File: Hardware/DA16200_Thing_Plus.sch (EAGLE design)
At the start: 61 parts, among them J2 THING_PLUS, J3 Qwiic, J5 USB C, J6 microSD, J7 CORTEX_JTAG_DEBUG_PTH_NS, Q1 20V/4.2A/52mΩ/1.4W, U1 DA16200MOD, U2 CH340E_MSOP10, U3 MCP73831, U5 4MB Flash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

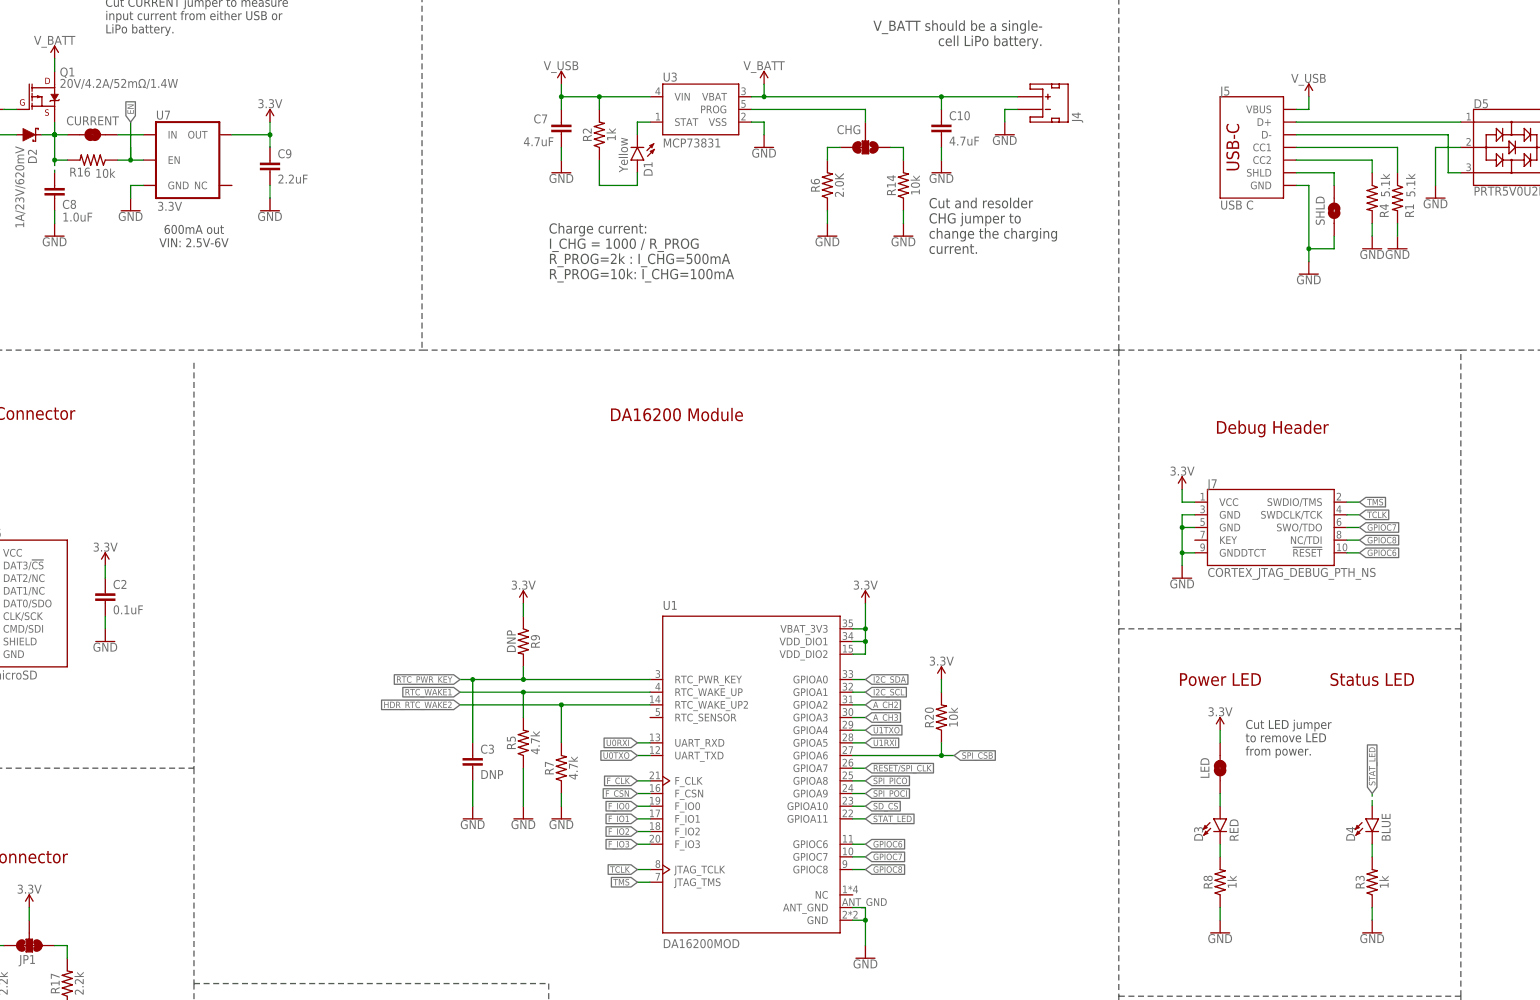
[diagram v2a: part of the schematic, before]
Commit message: Design review updates
Schematic:
* Re-wire wakeup pins to match app schematic and previous designs
* Change SHLD jumper to NC
* Remove "ANT_GND" pin label from DA16200 symbol
Board:
* Draw polygon to connect shield pins of USBC connector on top and bottom
* Rename button GPIOC7
* Breakout JTAG pins to TPs on the bottom
* Redraw polygons for middle layers to avoid the antenna GND keepout
* Fixed LED label on the jumper and the pin
* Changed "CURR" label to "MEAS"
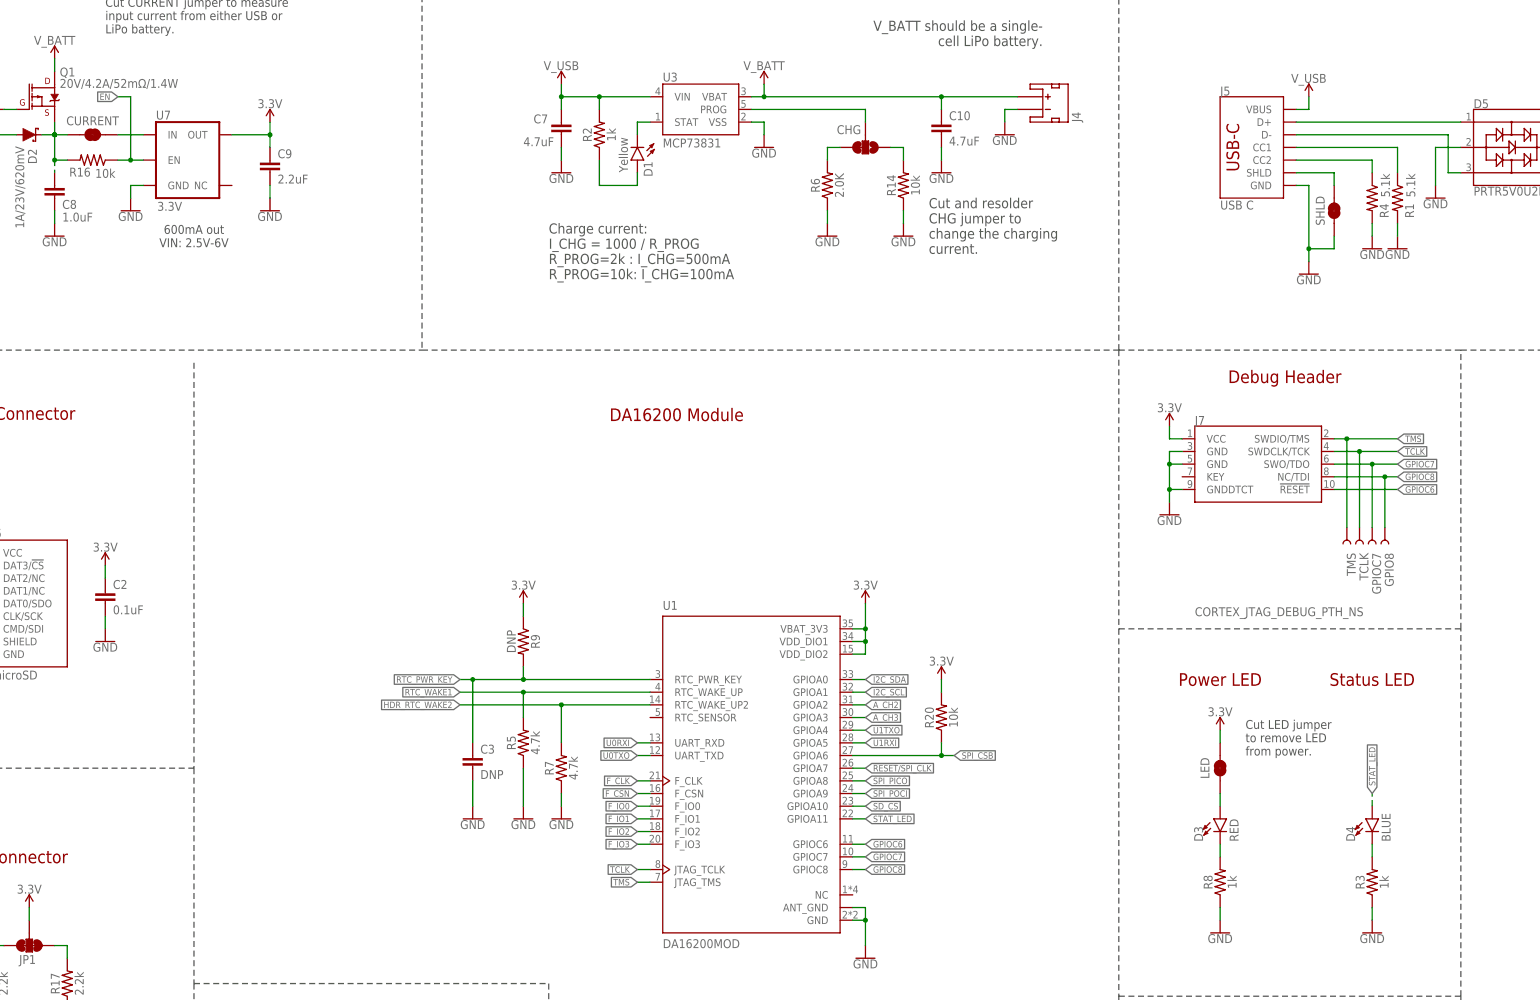
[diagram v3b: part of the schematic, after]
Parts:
- added GPIO8, GPIOC7, TCLK, TMS: TEST-POINT3, SparkFun-Connectors:TEST-POINT3
- SHLD: value JUMPER-SMT_2_NO_SILK -> JUMPER-SMT_2_NC_TRACE_SILK; device SparkFun-Jumpers:JUMPER-SMT_2_NO_SILK -> SparkFun-Jumpers:JUMPER-SMT_2_NC_TRACE_SILK
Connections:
- net GPIOC7: now also GPIOC7.1
- net GPIOC8: now also GPIO8.1
- net TCLK: now also TCLK.1
- net TMS: now also TMS.1
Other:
- moved on the sheet: J7
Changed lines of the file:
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@@
 <?xml version="1.0" encoding="utf-8"?>
 <!DOCTYPE eagle SYSTEM "eagle.dtd">
-<eagle version="9.5.2">
+<eagle version="9.4.2">
 <drawing>
 <settings>
-<setting alwaysvectorfont="no"/>
+<setting alwaysvectorfont="yes"/>
 <setting keepoldvectorfont="yes"/>
 <setting verticaltext="up"/>
@@
 <part name="GND22" library="SparkFun-PowerSymbols" deviceset="GND" device=""/>
 <part name="R18" library="SparkFun-Resistors" deviceset="100OHM" device="-0402-TIGHT-1/16W-1%" value="100"/>
-<part name="SHLD" library="SparkFun-Jumpers" deviceset="JUMPER-SMT_2_NO" device="_SILK" package3d_urn="urn:adsk.eagle:package:39279/1"/>
+<part name="SHLD" library="SparkFun-Jumpers" deviceset="JUMPER-SMT_2_NC_TRACE" device="_SILK" package3d_urn="urn:adsk.eagle:package:39281/1"/>
 <part name="GND23" library="SparkFun-PowerSymbols" deviceset="GND" device=""/>
 <part name="GND24" library="SparkFun-PowerSymbols" deviceset="GND" device=""/>
@@
 <part name="SUPPLY18" library="SparkFun-PowerSymbols" deviceset="3.3V" device=""/>
 <part name="SUPPLY19" library="SparkFun-PowerSymbols" deviceset="3.3V" device=""/>
+<part name="TMS" library="SparkFun-Connectors" deviceset="TEST-POINT" device="3"/>
+<part name="TCLK" library="SparkFun-Connectors" deviceset="TEST-POINT" device="3"/>
+<part name="GPIOC7" library="SparkFun-Connectors" deviceset="TEST-POINT" device="3"/>
+<part name="GPIO8" library="SparkFun-Connectors" deviceset="TEST-POINT" device="3"/>
 </parts>
 <sheets>
@@
 <text x="40.64" y="180.34" size="2.54" layer="94" font="vector" align="center">uSD Connector</text>
 <wire x1="261.62" y1="193.04" x2="261.62" y2="279.4" width="0.2032" layer="97" style="longdash"/>
-<text x="292.354" y="177.546" size="2.54" layer="94" font="vector" align="center">Debug Header</text>
+<text x="294.894" y="187.706" size="2.54" layer="94" font="vector" align="center">Debug Header</text>
 <text x="281.94" y="127" size="2.54" layer="94" font="vector" align="center">Power LED</text>
 <text x="355.6" y="10.16" size="2.54" layer="94" font="vector">Priyanka Makin</text>
@@
 <attribute name="VALUE" x="421.64" y="228.346" size="1.778" layer="96" align="top-center"/>
 </instance>
-<instance part="J7" gate="J1" x="292.1" y="157.48" smashed="yes">
-<attribute name="NAME" x="279.4" y="165.354" size="1.778" layer="95" font="vector"/>
-<attribute name="VALUE" x="279.4" y="147.574" size="1.778" layer="96" font="vector"/>
-</instance>
-<instance part="SUPPLY13" gate="G$1" x="274.32" y="165.1" smashed="yes">
-<attribute name="VALUE" x="274.32" y="167.894" size="1.778" layer="96" align="bottom-center"/>
-</instance>
-<instance part="GND16" gate="1" x="274.32" y="147.32" smashed="yes">
-<attribute name="VALUE" x="274.32" y="147.066" size="1.778" layer="96" align="top-center"/>
+<instance part="J7" gate="J1" x="289.56" y="170.18" smashed="yes">
+<attribute name="NAME" x="276.86" y="178.054" size="1.778" layer="95" font="vector"/>
+<attribute name="VALUE" x="276.86" y="139.7" size="1.778" layer="96" font="vector"/>
+</instance>
+<instance part="SUPPLY13" gate="G$1" x="271.78" y="177.8" smashed="yes">
+<attribute name="VALUE" x="271.78" y="180.594" size="1.778" layer="96" align="bottom-center"/>
+</instance>
+<instance part="GND16" gate="1" x="271.78" y="160.02" smashed="yes">
+<attribute name="VALUE" x="271.78" y="159.766" size="1.778" layer="96" align="top-center"/>
 </instance>
 <instance part="R5" gate="G$1" x="142.24" y="114.3" smashed="yes" rot="R90">
@@
 <instance part="SUPPLY19" gate="G$1" x="226.06" y="127" smashed="yes">
 <attribute name="VALUE" x="226.06" y="129.794" size="1.778" layer="96" align="bottom-center"/>
+</instance>
+<instance part="TMS" gate="G$1" x="307.34" y="157.48" smashed="yes" rot="R270">
+<attribute name="NAME" x="307.34" y="152.4" size="1.778" layer="95" font="vector" rot="R270"/>
+</instance>
+<instance part="TCLK" gate="G$1" x="309.88" y="157.48" smashed="yes" rot="R270">
+<attribute name="NAME" x="309.88" y="152.4" size="1.778" layer="95" font="vector" rot="R270"/>
+</instance>
+<instance part="GPIOC7" gate="G$1" x="312.42" y="157.48" smashed="yes" rot="R270">
+<attribute name="NAME" x="312.42" y="152.4" size="1.778" layer="95" font="vector" rot="R270"/>
+</instance>
+<instance part="GPIO8" gate="G$1" x="314.96" y="157.48" smashed="yes" rot="R270">
+<attribute name="NAME" x="314.96" y="152.4" size="1.778" layer="95" font="vector" rot="R270"/>
 </instance>
 </instances>
@@
 <segment>
 <pinref part="J7" gate="J1" pin="VCC"/>
-<wire x1="276.86" y1="162.56" x2="274.32" y2="162.56" width="0.1524" layer="91"/>
-<wire x1="274.32" y1="162.56" x2="274.32" y2="165.1" width="0.1524" layer="91"/>
+<wire x1="274.32" y1="175.26" x2="271.78" y2="175.26" width="0.1524" layer="91"/>
+<wire x1="271.78" y1="175.26" x2="271.78" y2="177.8" width="0.1524" layer="91"/>
 <pinref part="SUPPLY13" gate="G$1" pin="3.3V"/>
 </segment>
@@
 <segment>
 <pinref part="J7" gate="J1" pin="GND@3"/>
-<wire x1="276.86" y1="160.02" x2="274.32" y2="160.02" width="0.1524" layer="91"/>
-<wire x1="274.32" y1="160.02" x2="274.32" y2="157.48" width="0.1524" layer="91"/>
+<wire x1="274.32" y1="172.72" x2="271.78" y2="172.72" width="0.1524" layer="91"/>
+<wire x1="271.78" y1="172.72" x2="271.78" y2="170.18" width="0.1524" layer="91"/>
 <pinref part="J7" gate="J1" pin="GND@5"/>
-<wire x1="274.32" y1="157.48" x2="274.32" y2="152.4" width="0.1524" layer="91"/>
-<wire x1="274.32" y1="152.4" x2="274.32" y2="149.86" width="0.1524" layer="91"/>
-<wire x1="276.86" y1="157.48" x2="274.32" y2="157.48" width="0.1524" layer="91"/>
-<junction x="274.32" y="157.48"/>
+<wire x1="271.78" y1="170.18" x2="271.78" y2="165.1" width="0.1524" layer="91"/>
+<wire x1="271.78" y1="165.1" x2="271.78" y2="162.56" width="0.1524" layer="91"/>
+<wire x1="274.32" y1="170.18" x2="271.78" y2="170.18" width="0.1524" layer="91"/>
+<junction x="271.78" y="170.18"/>
 <pinref part="J7" gate="J1" pin="GNDDTCT"/>
-<wire x1="274.32" y1="152.4" x2="276.86" y2="152.4" width="0.1524" layer="91"/>
-<junction x="274.32" y="152.4"/>
+<wire x1="271.78" y1="165.1" x2="274.32" y2="165.1" width="0.1524" layer="91"/>
+<junction x="271.78" y="165.1"/>
 <pinref part="GND16" gate="1" pin="GND"/>
 </segment>
@@
 <segment>
 <wire x1="66.04" y1="231.14" x2="63.5" y2="231.14" width="0.1524" layer="91"/>
-<wire x1="63.5" y1="231.14" x2="60.96" y2="231.14" width="0.1524" layer="91"/>
-<wire x1="63.5" y1="238.76" x2="63.5" y2="231.14" width="0.1524" layer="91"/>
-<wire x1="63.5" y1="233.68" x2="63.5" y2="231.14" width="0.1524" layer="91"/>
-<junction x="63.5" y="231.14"/>
-<label x="63.5" y="238.76" size="1.27" layer="95" font="vector" rot="R90" xref="yes"/>
 <pinref part="U7" gate="G$1" pin="EN"/>
 <pinref part="R16" gate="G$1" pin="1"/>
+<wire x1="63.5" y1="231.14" x2="60.96" y2="231.14" width="0.1524" layer="91"/>
+<wire x1="63.5" y1="231.14" x2="63.5" y2="243.84" width="0.1524" layer="91"/>
+<junction x="63.5" y="231.14"/>
+<wire x1="63.5" y1="243.84" x2="60.96" y2="243.84" width="0.1524" layer="91"/>
+<label x="60.96" y="243.84" size="1.27" layer="95" rot="R180" xref="yes"/>
 </segment>
 <segment>
@@
 <segment>
 <pinref part="J7" gate="J1" pin="!RESET"/>
-<wire x1="307.34" y1="152.4" x2="309.88" y2="152.4" width="0.1524" layer="91"/>
-<label x="309.88" y="152.4" size="1.27" layer="95" xref="yes"/>
+<wire x1="304.8" y1="165.1" x2="317.5" y2="165.1" width="0.1524" layer="91"/>
+<label x="317.5" y="165.1" size="1.27" layer="95" xref="yes"/>
 </segment>
 <segment>
@@
 <segment>
 <pinref part="J7" gate="J1" pin="SWO/TDO"/>
-<wire x1="307.34" y1="157.48" x2="309.88" y2="157.48" width="0.1524" layer="91"/>
-<label x="309.88" y="157.48" size="1.27" layer="95" xref="yes"/>
+<wire x1="304.8" y1="170.18" x2="312.42" y2="170.18" width="0.1524" layer="91"/>
+<label x="317.5" y="170.18" size="1.27" layer="95" xref="yes"/>
+<pinref part="GPIOC7" gate="G$1" pin="1"/>
+<wire x1="312.42" y1="170.18" x2="317.5" y2="170.18" width="0.1524" layer="91"/>
+<wire x1="312.42" y1="157.48" x2="312.42" y2="170.18" width="0.1524" layer="91"/>
+<junction x="312.42" y="170.18"/>
 </segment>
 </net>
@@
 <segment>
 <pinref part="J7" gate="J1" pin="NC/TDI"/>
-<wire x1="307.34" y1="154.94" x2="309.88" y2="154.94" width="0.1524" layer="91"/>
-<label x="309.88" y="154.94" size="1.27" layer="95" xref="yes"/>
+<wire x1="304.8" y1="167.64" x2="314.96" y2="167.64" width="0.1524" layer="91"/>
+<label x="317.5" y="167.64" size="1.27" layer="95" xref="yes"/>
+<pinref part="GPIO8" gate="G$1" pin="1"/>
+<wire x1="314.96" y1="167.64" x2="317.5" y2="167.64" width="0.1524" layer="91"/>
+<wire x1="314.96" y1="157.48" x2="314.96" y2="167.64" width="0.1524" layer="91"/>
+<junction x="314.96" y="167.64"/>
 </segment>
 </net>
@@
 <segment>
 <pinref part="J7" gate="J1" pin="SWDIO/TMS"/>
-<wire x1="307.34" y1="162.56" x2="309.88" y2="162.56" width="0.1524" layer="91"/>
-<label x="309.88" y="162.56" size="1.27" layer="95" xref="yes"/>
+<wire x1="304.8" y1="175.26" x2="307.34" y2="175.26" width="0.1524" layer="91"/>
+<label x="317.5" y="175.26" size="1.27" layer="95" xref="yes"/>
+<pinref part="TMS" gate="G$1" pin="1"/>
+<wire x1="307.34" y1="175.26" x2="317.5" y2="175.26" width="0.1524" layer="91"/>
+<wire x1="307.34" y1="157.48" x2="307.34" y2="175.26" width="0.1524" layer="91"/>
+<junction x="307.34" y="175.26"/>
 </segment>
 <segment>
@@
 <segment>
 <pinref part="J7" gate="J1" pin="SWDCLK/TCK"/>
-<wire x1="307.34" y1="160.02" x2="309.88" y2="160.02" width="0.1524" layer="91"/>
-<label x="309.88" y="160.02" size="1.27" layer="95" xref="yes"/>
-</segment>
-<segment>
+<wire x1="304.8" y1="172.72" x2="309.88" y2="172.72" width="0.1524" layer="91"/>
+<label x="317.5" y="172.72" size="1.27" layer="95" xref="yes"/>
+<pinref part="TCLK" gate="G$1" pin="1"/>
+<wire x1="309.88" y1="172.72" x2="317.5" y2="172.72" width="0.1524" layer="91"/>
+<wire x1="309.88" y1="157.48" x2="309.88" y2="172.72" width="0.1524" layer="91"/>
+<junction x="309.88" y="172.72"/>
+</segment>
+<segment>
